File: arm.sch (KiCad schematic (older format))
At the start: 96 parts, among them J1 MICROSD_SOCKET_SPI, M1 MOTOR, P1 MicroUSB, P2 HC-05/06, Q1 MOSFET_N, Q2 IRLML2246TRPBF, Q3 IRLML2246TRPBF, Q5 IRLML2246TRPBF, Q6 IRLML2246TRPBF, Q7 IRLML2246TRPBF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

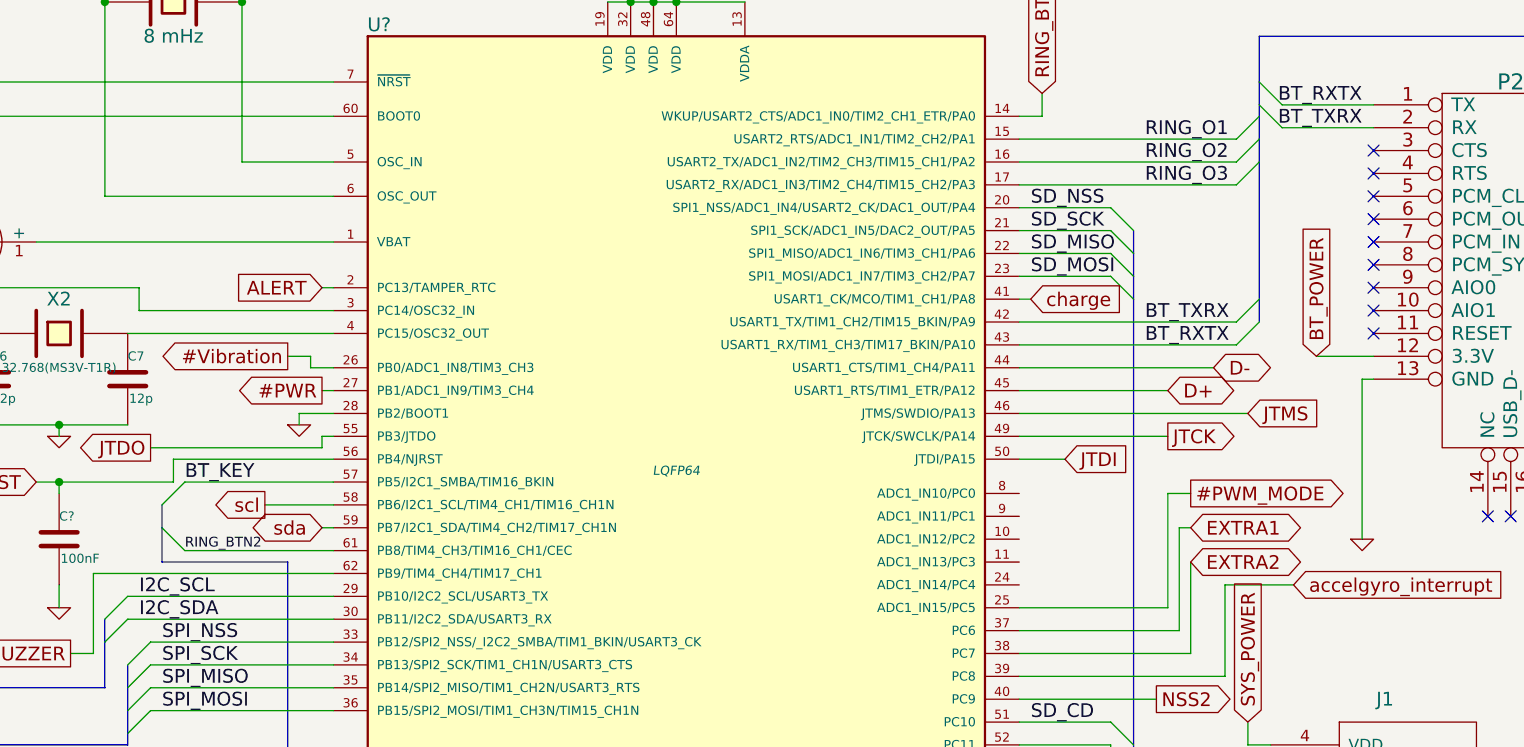
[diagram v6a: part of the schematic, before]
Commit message: BT_KEY is now near to other BT pins
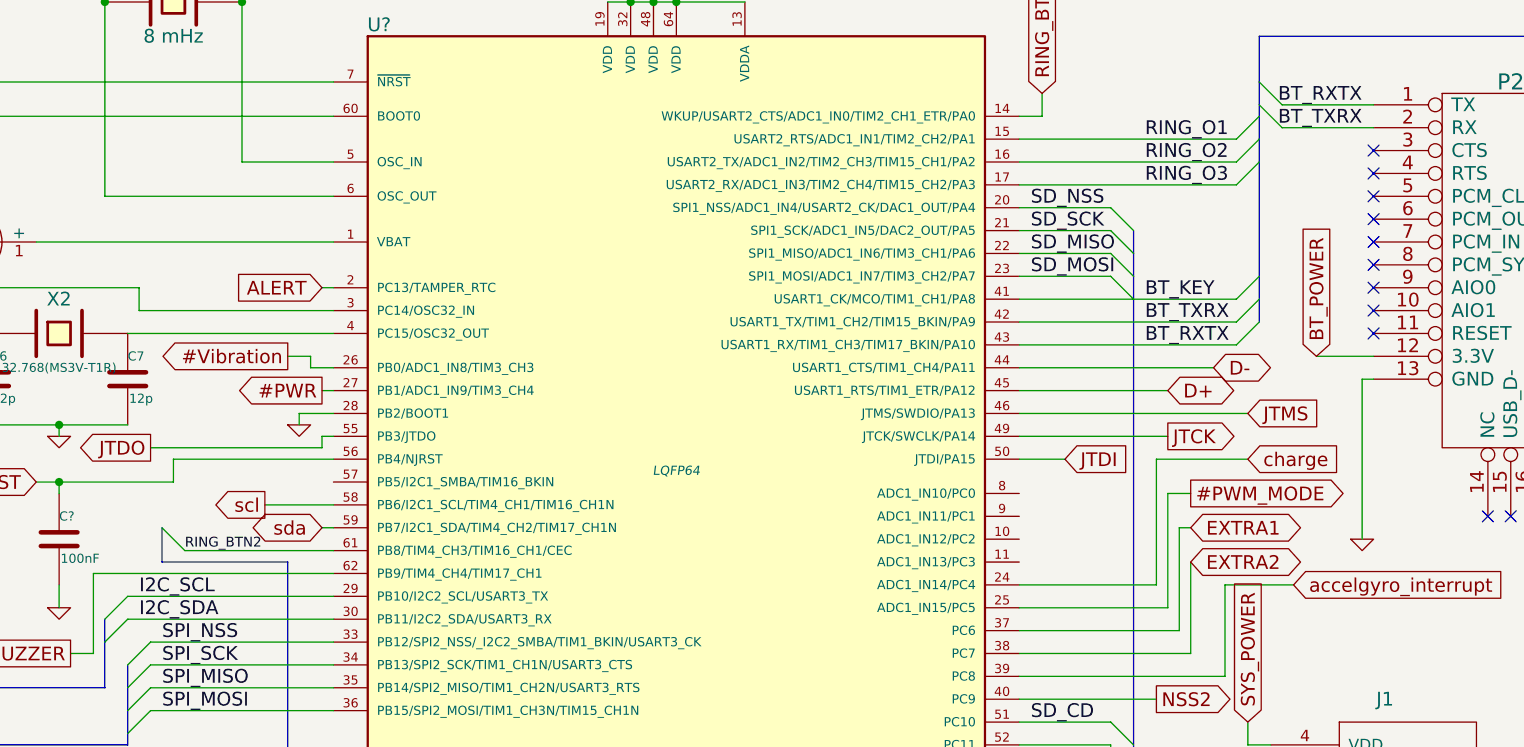
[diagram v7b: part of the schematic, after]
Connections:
- net BT_KEY: now also U?.41 (USART1_CK/MCO/TIM1_CH1/PA8); no longer U?.57 (PB5/I2C1_SMBA/TIM16_BKIN)
- net charge: now also U?.24 (ADC1_IN14/PC4); no longer U?.41 (USART1_CK/MCO/TIM1_CH1/PA8)
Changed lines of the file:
@@
 	1    0    0    -1
 $EndComp
-Text GLabel 7150 2450 2    60   Input ~ 0
-charge
 Text GLabel 10500 5200 3    60   Output ~ 0
 charge
@@
 Text GLabel 1000 3800 3    60   Output ~ 0
 scl
-Text Label 3450 3250 0    60   ~ 0
-BT_KEY
-Entry Wire Line
-	3350 3350 3450 3250
 $Comp
 L R R17
@@
 	3350 3600 3900 3600
 Wire Wire Line
-	3450 3250 4100 3250
-Wire Wire Line
 	4050 3450 4100 3450
 Wire Wire Line
@@
 	8150 1750 8150 1850
 Wire Bus Line
-	8150 1850 8150 2450
+	8150 1850 8150 2350
+Wire Bus Line
+	8150 2350 8150 2450
 Wire Bus Line
 	8150 2450 8150 2550
@@
 	7100 2550 8050 2550
 Wire Wire Line
-	7150 2450 7100 2450
+	7100 2450 7600 2450
+Wire Wire Line
+	7600 2450 8050 2450
 Wire Wire Line
 	700  1250 1050 1250
@@
 	1950 4250 1950 4350
 Wire Bus Line
-	3350 3350 3350 3450
-Wire Bus Line
 	3350 3450 3350 3600
 Wire Wire Line
@@
 	1    0    0    -1
 $EndComp
+Entry Wire Line
+	8050 2450 8150 2350
+Text Label 7650 2450 0    60   ~ 0
+BT_KEY
+Wire Wire Line
+	8100 3150 7700 3150
+Wire Wire Line
+	7700 3150 7700 3700
+Wire Wire Line
+	7700 3700 7100 3700
+Text GLabel 8100 3150 2    60   Input ~ 0
+charge
 $EndSCHEMATC

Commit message: RING_BTN2 on PC1
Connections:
- net RING_BTN2: now also U?.9 (ADC1_IN11/PC1); no longer U?.61 (PB8/TIM4_CH3/TIM16_CH1/CEC)
